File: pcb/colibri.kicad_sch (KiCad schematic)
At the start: 91 parts

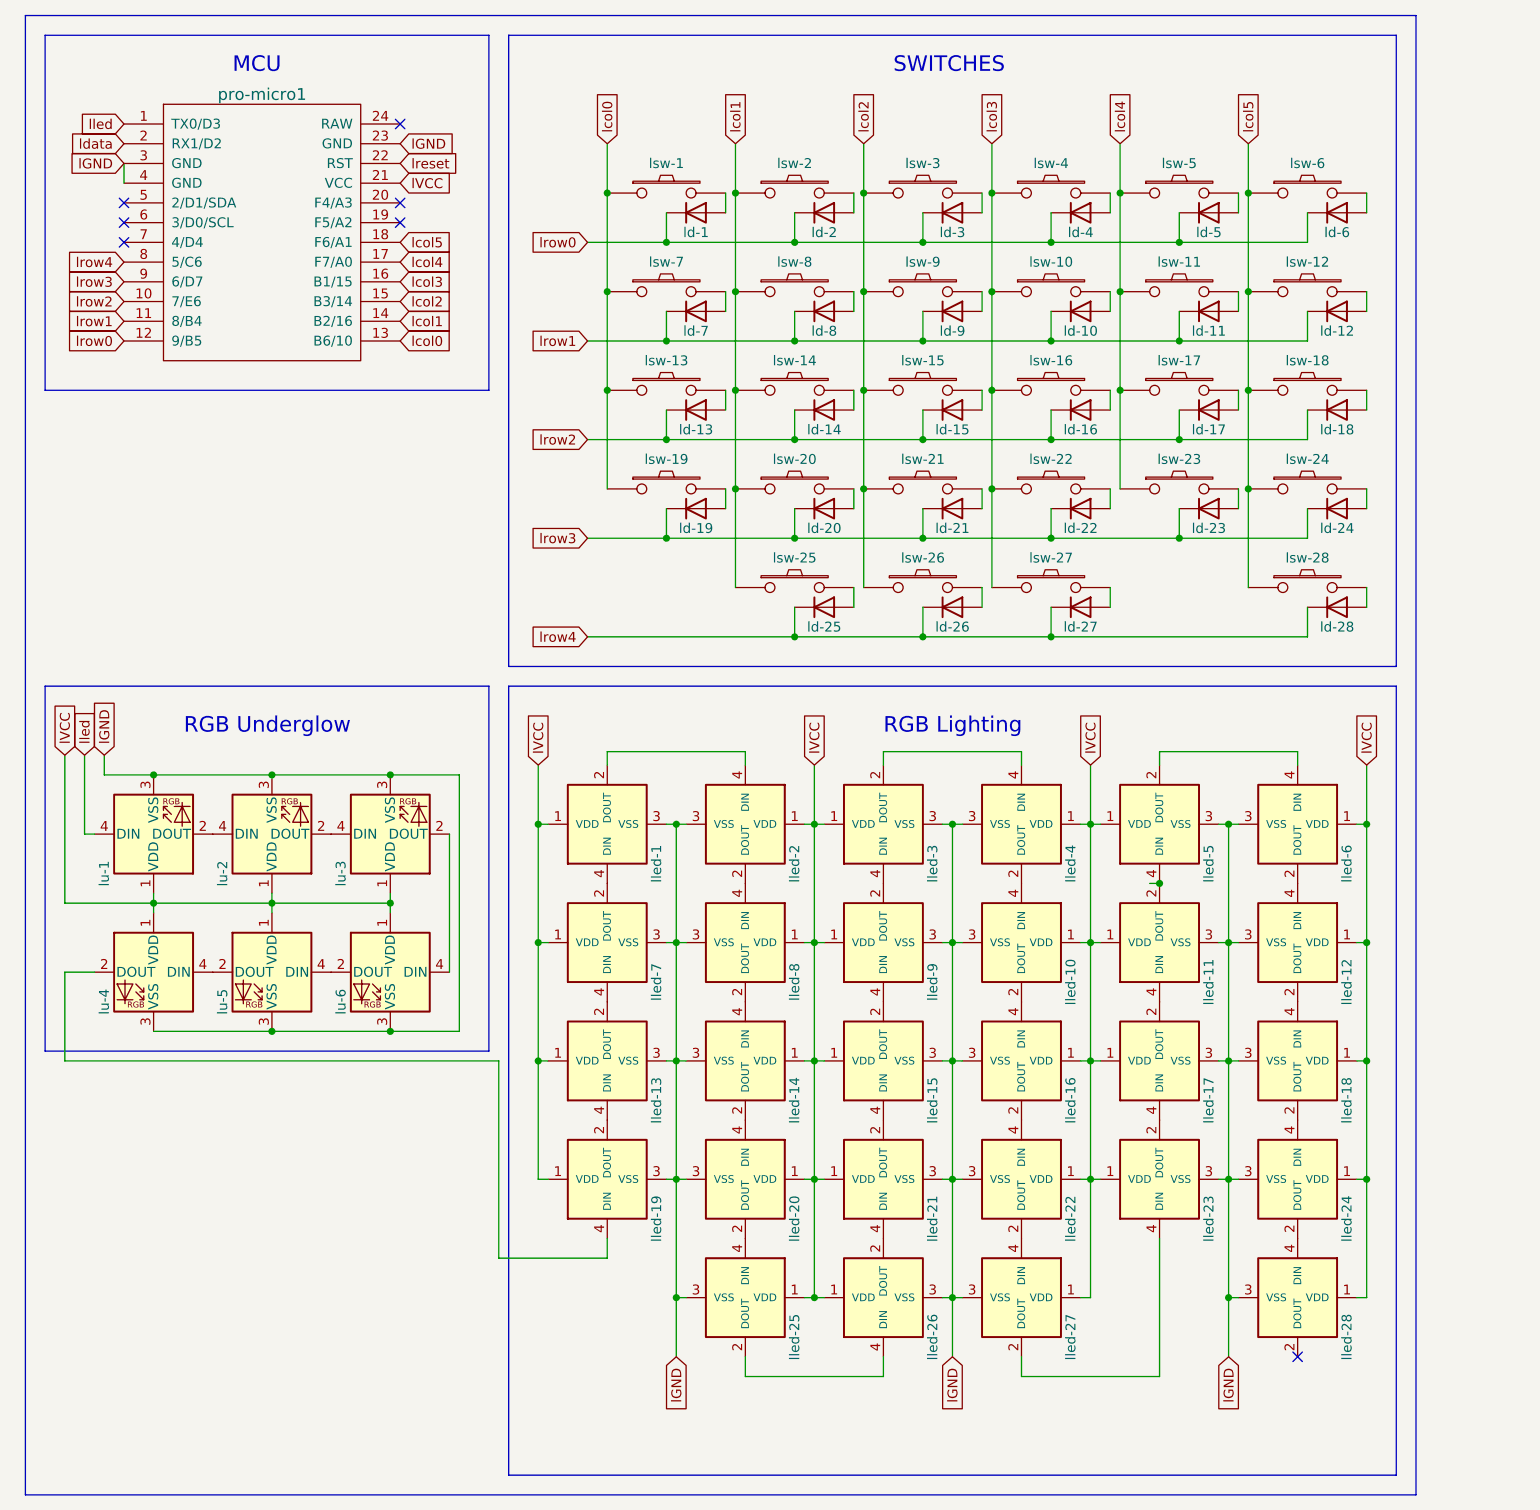
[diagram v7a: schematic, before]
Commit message: all keys connected
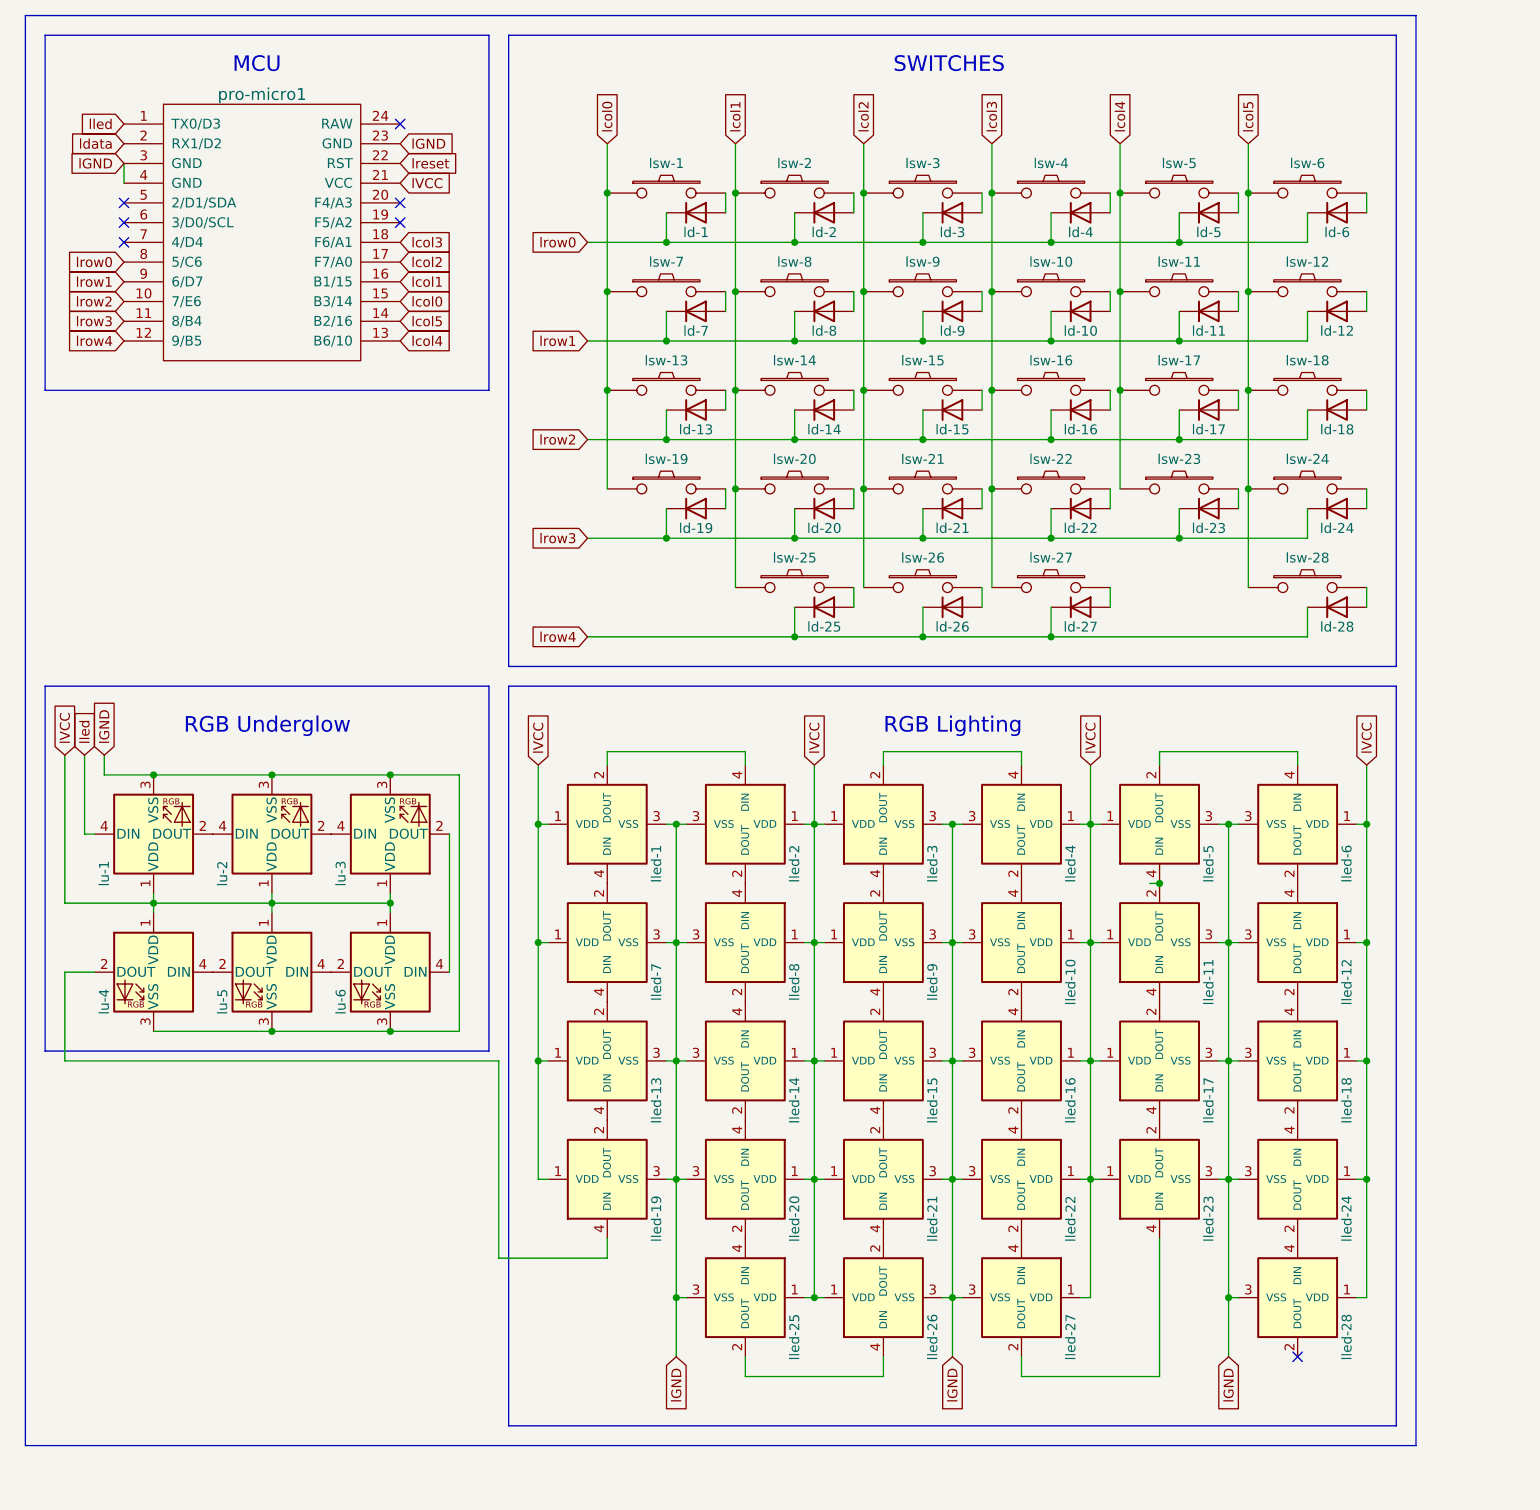
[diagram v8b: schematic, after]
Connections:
- net lcol0: now also pro-micro1.15 (B3/14); no longer pro-micro1.13 (B6/10)
- net lcol1: now also pro-micro1.16 (B1/15); no longer pro-micro1.14 (B2/16)
- net lcol2: now also pro-micro1.17 (F7/A0); no longer pro-micro1.15 (B3/14)
- net lcol3: now also pro-micro1.18 (F6/A1); no longer pro-micro1.16 (B1/15)
- net lcol4: now also pro-micro1.13 (B6/10); no longer pro-micro1.17 (F7/A0)
- net lcol5: now also pro-micro1.14 (B2/16); no longer pro-micro1.18 (F6/A1)
- net lrow0: now also pro-micro1.8 (5/C6); no longer pro-micro1.12 (9/B5)
- net lrow1: now also pro-micro1.9 (6/D7); no longer pro-micro1.11 (8/B4)
- net lrow3: now also pro-micro1.11 (8/B4); no longer pro-micro1.9 (6/D7)
- net lrow4: now also pro-micro1.12 (9/B5); no longer pro-micro1.8 (5/C6)
